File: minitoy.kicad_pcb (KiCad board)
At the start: 4 copper layers, 47.2 x 45 mm, 49 parts, among them J1 Conn_01x06, J2 PMOD1, J3 PMOD2, J4 USB_B_Micro, J5 PMOD3, U1 ICE40UP5K-SG48, U2 ESP-12E, U3 MIC5504-1.2YM5, U4 MIC5504-3.3YM5, U5 MIC5504-3.3YM5

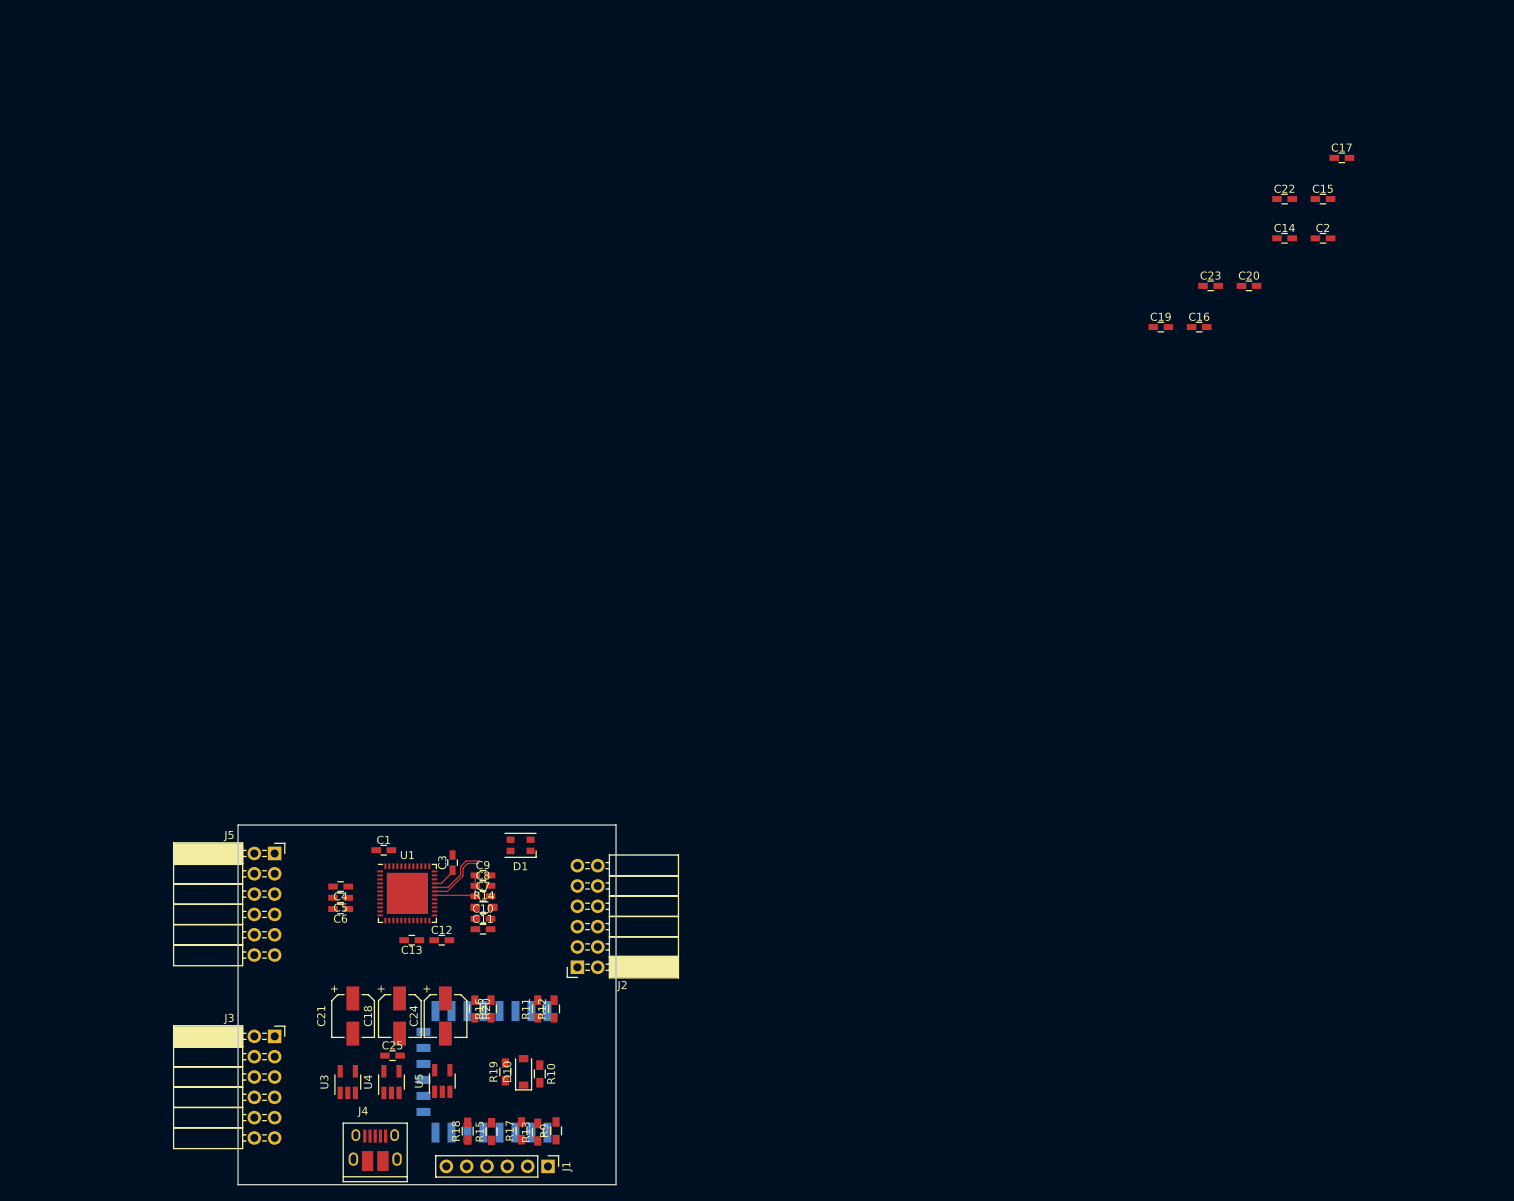
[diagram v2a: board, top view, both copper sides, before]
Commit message: More layout changes, remove a PMOD socket for easier routing
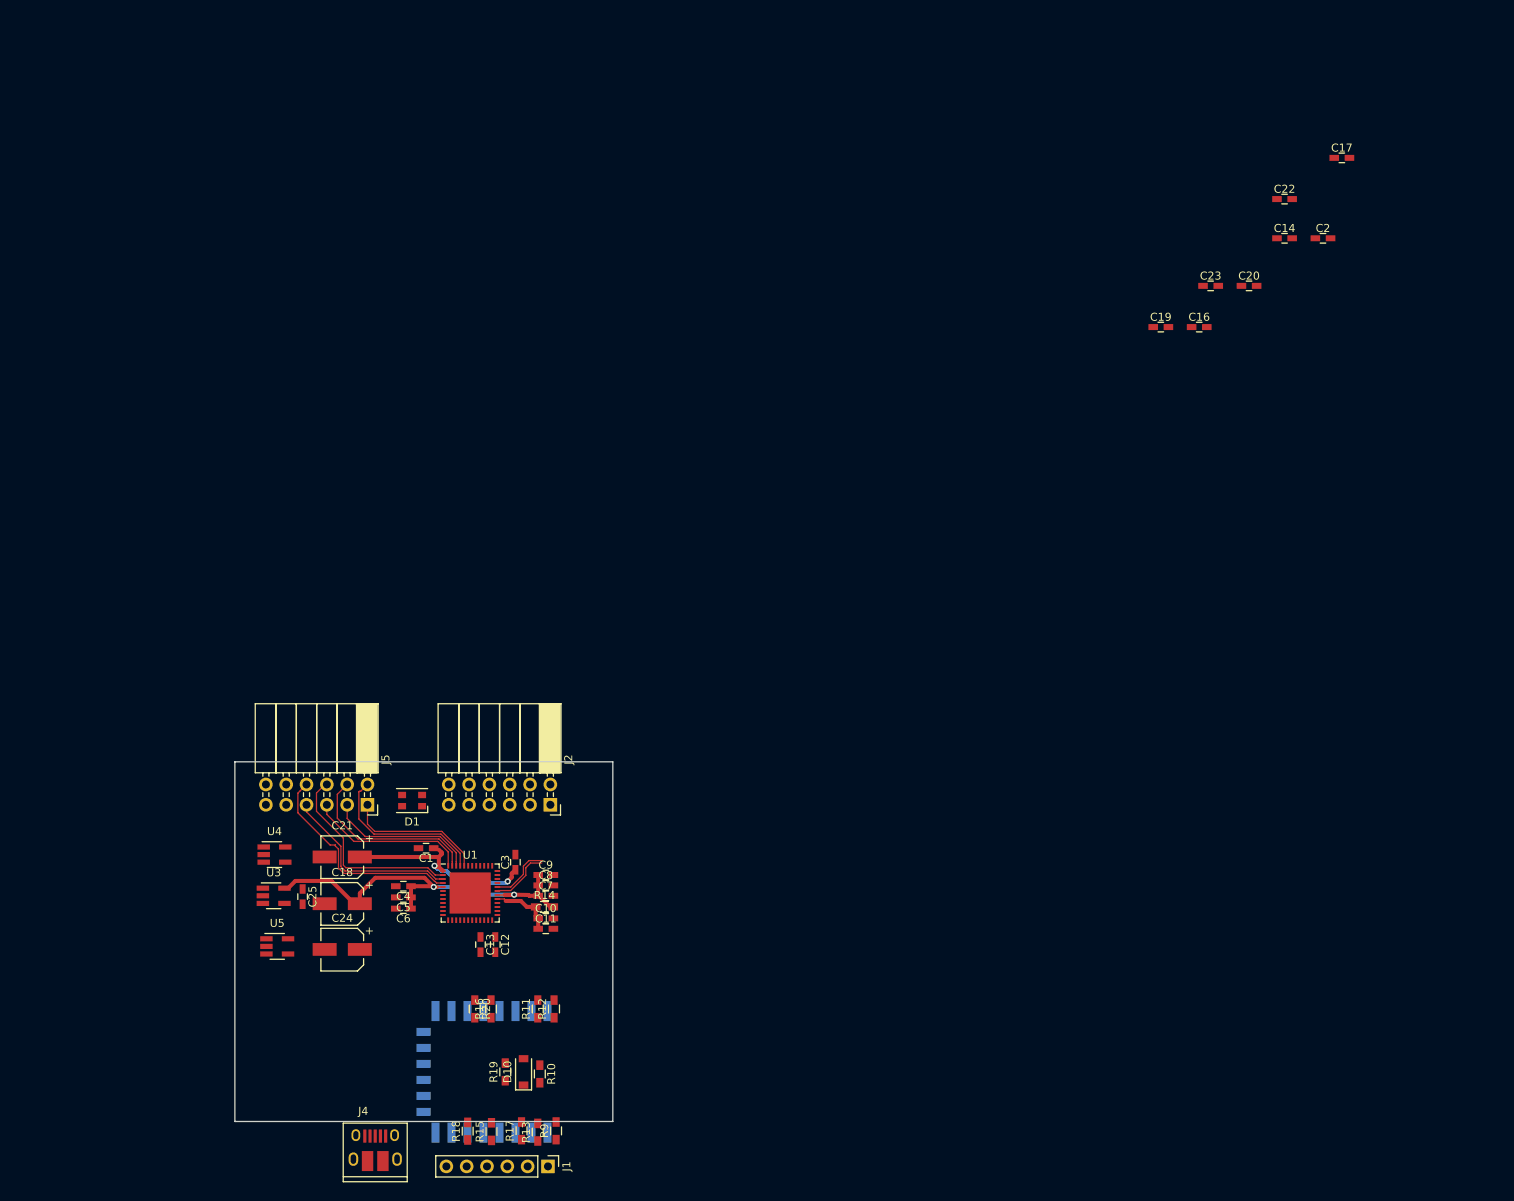
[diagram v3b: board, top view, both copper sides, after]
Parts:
- removed C15: 0.1uF, Capacitors_SMD:C_0603_HandSoldering
- removed J3: PMOD2, Socket_Strips:Socket_Strip_Angled_2x06_Pitch2.54mm
- J5: value PMOD3 -> PMOD2
- moved U4 32.0 mm to (96.5, 111.9), turned to 0 degrees
- moved U5 26.6 mm to (96.8, 123.4), turned to 0 degrees
- moved U3 25.1 mm to (96.4, 117.0), turned to 0 degrees
- moved C25 22.8 mm to (100.0, 117.2), turned to 270 degrees
- moved J2 20.6 mm to (131.0, 105.7), turned to 270 degrees
- moved C21 19.9 mm to (105.0, 112.2), turned to 180 degrees
- moved C18 15.8 mm to (105.0, 118.0), turned to 180 degrees
- moved C24 15.3 mm to (105.0, 123.8), turned to 180 degrees
- moved D1 14.7 mm to (113.7, 105.2)
- moved J5 13.1 mm to (108.1, 105.7), turned to 270 degrees
- moved C13 8.61 mm to (122.2, 123.2), turned to 270 degrees
- moved C10 7.85 mm to (130.4, 119.9)
- moved C11 7.85 mm to (130.4, 121.2)
- moved C7 7.85 mm to (130.4, 117.1)
- moved C8 7.85 mm to (130.4, 115.8)
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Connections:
- net Net-(C10-Pad1) renamed /VCCPLL
- J5 pad 1: PMOD-3.1 -> PMOD-2.1
- J5 pad 2: PMOD-3.7 -> PMOD-2.7
- J5 pad 3: PMOD-3.2 -> PMOD-2.2
- J5 pad 4: PMOD-3.8 -> PMOD-2.8
- J5 pad 5: PMOD-3.3 -> PMOD-2.3
- J5 pad 6: PMOD-3.9 -> PMOD-2.9
- J5 pad 7: PMOD-3.4 -> PMOD-2.4
- J5 pad 8: PMOD-3.10 -> PMOD-2.10
- U1 pad 10: PMOD-2.3 -> Net-(U1-Pad10)
- U1 pad 11: PMOD-2.4 -> Net-(U1-Pad11)
- U1 pad 12: PMOD-2.7 -> Net-(U1-Pad12)
- U1 pad 13: PMOD-2.8 -> Net-(U1-Pad13)
- U1 pad 18: PMOD-2.9 -> Net-(U1-Pad18)
- U1 pad 19: PMOD-2.10 -> Net-(U1-Pad19)
- U1 pad 2: PMOD-3.8 -> PMOD-2.9
- U1 pad 3: PMOD-3.9 -> PMOD-2.4
- U1 pad 4: PMOD-3.10 -> PMOD-2.10
- U1 pad 44: PMOD-3.1 -> PMOD-2.1
- U1 pad 45: PMOD-3.2 -> PMOD-2.7
- U1 pad 46: PMOD-3.3 -> PMOD-2.2
- U1 pad 47: PMOD-3.4 -> PMOD-2.8
- U1 pad 48: PMOD-3.7 -> PMOD-2.3
- U1 pad 6: PMOD-2.1 -> Net-(U1-Pad6)
- U1 pad 9: PMOD-2.2 -> Net-(U1-Pad9)
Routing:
- net +1V2: track 7.74 -> 50.3 mm, vias 0 -> 2
- net PMOD-2.10: track 0.00 -> 27.2 mm
- net PMOD-2.9: track 0.00 -> 25.1 mm
- net PMOD-2.4: track 0.00 -> 22.9 mm
- net PMOD-2.8: track 0.00 -> 22.6 mm
- net +3V3: track 3.07 -> 25.6 mm, vias 0 -> 2
- net PMOD-2.7: track 0.00 -> 20.9 mm
- net PMOD-2.3: track 0.00 -> 20.0 mm
- net PMOD-2.2: track 0.00 -> 18.7 mm
- net PMOD-2.1: track 0.00 -> 17.5 mm
- net /VCCPLL: track 0.00 -> 8.02 mm
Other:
- net class PWR: clearance 0.254 -> 0.1524

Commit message: Routing done, but cleanup needed
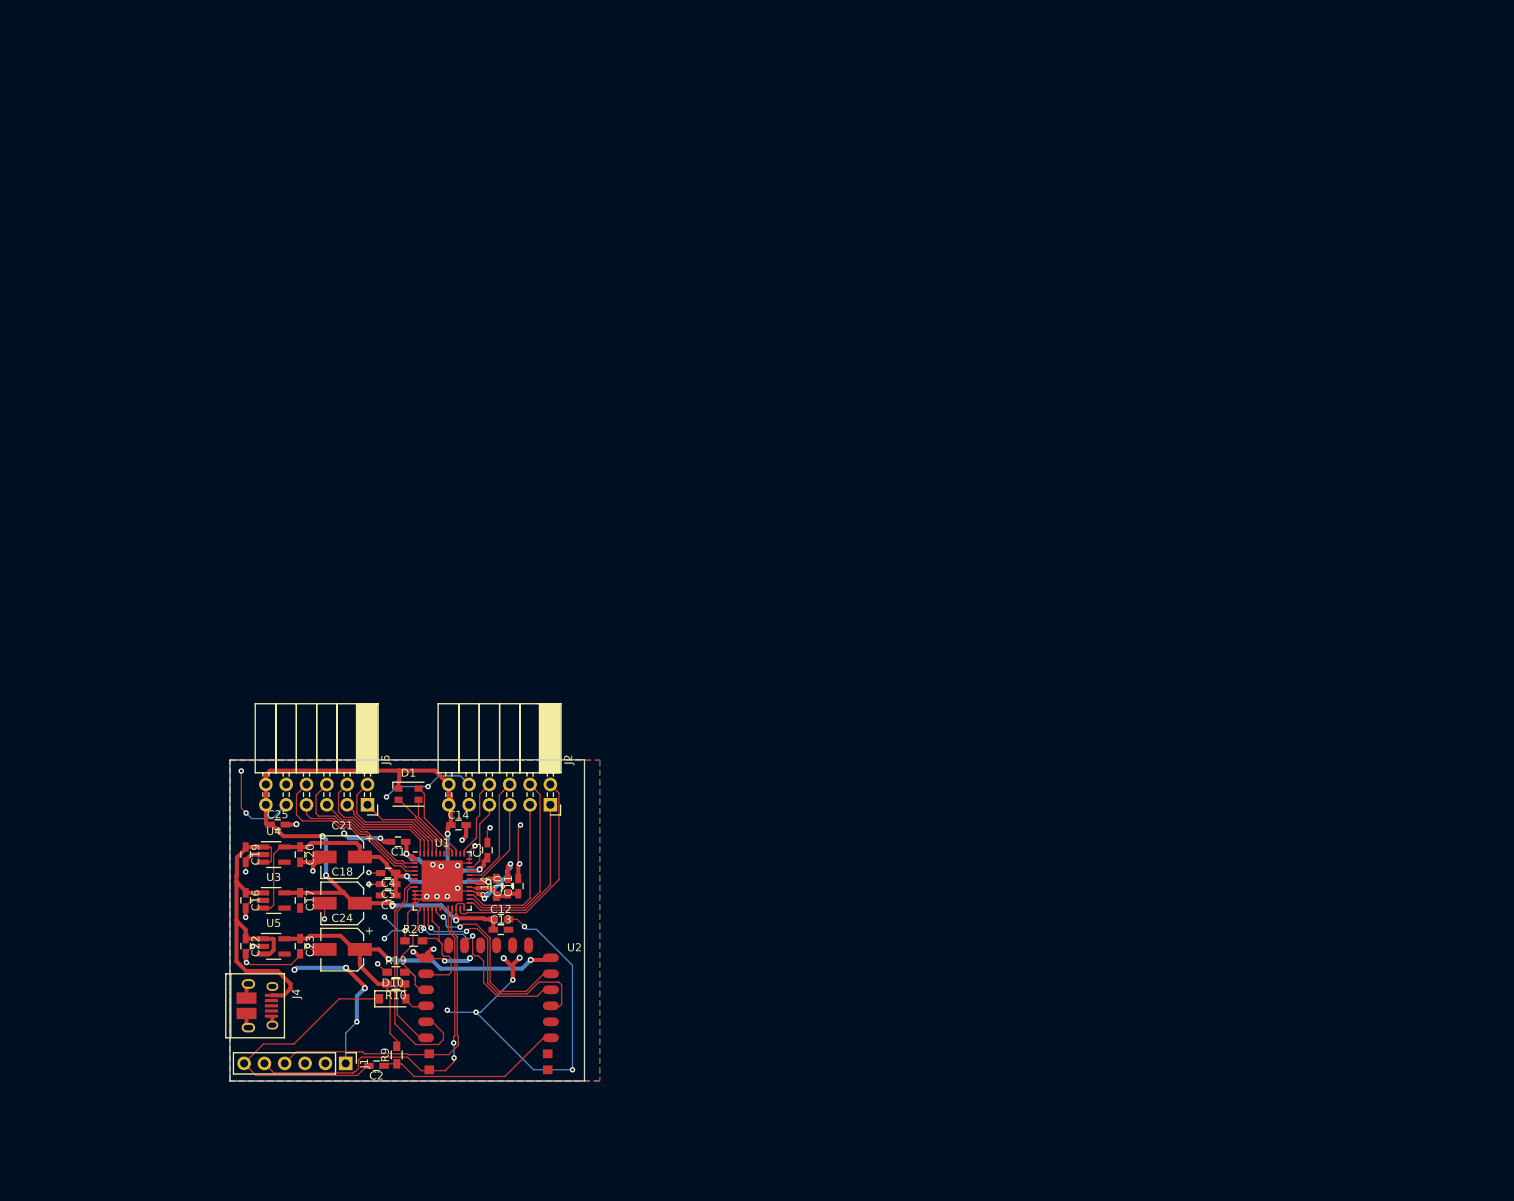
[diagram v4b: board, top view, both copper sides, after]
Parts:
- removed C7: 0.01uF, Capacitors_SMD:C_0603_HandSoldering
- removed C8: 0.1uF, Capacitors_SMD:C_0603_HandSoldering
- removed C9: 1uF, Capacitors_SMD:C_0603_HandSoldering
- removed R11, R12, R13, R15, R16, R17, R18: 100, Resistors_SMD:R_0603_HandSoldering
- C1, C13, C3: value 0.01uF -> 0.1uF
- U2: footprint RF_Modules:ESP-12E -> wifi_pants:ESP-12E-narrow; moved to F.Cu
- U3: value MIC5504-1.2YM5 -> MIC5504-3.3YM5
- U4: value MIC5504-3.3YM5 -> MIC5504-1.2YM5
- moved C22 160.0 mm to (92.9, 123.3), turned to 270 degrees
- moved C17 159.9 mm to (99.7, 117.6), turned to 270 degrees
- moved C2 157.2 mm to (109.2, 138.3), turned to 180 degrees
- moved C23 140.6 mm to (99.7, 123.3), turned to 270 degrees
- moved C16 139.1 mm to (92.9, 117.6), turned to 270 degrees
- moved C20 138.3 mm to (99.7, 111.9), turned to 270 degrees
- moved C19 132.0 mm to (92.9, 111.9), turned to 270 degrees
- moved C14 126.7 mm to (119.5, 108.2)
- moved J1 28.4 mm to (105.4, 138.0)
- moved J4 22.9 mm to (94.6, 130.8), turned to 270 degrees
- moved R9 22.1 mm to (111.8, 136.9)
- moved R10 21.2 mm to (111.7, 128.1), turned to 180 degrees
- moved D10 18.7 mm to (111.3, 129.9), turned to 0 degrees
- moved R19 18.5 mm to (111.7, 126.6), turned to 0 degrees
- moved R20 11.4 mm to (113.9, 122.7), turned to 0 degrees
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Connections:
- C17 pad 1: +1V2 -> +3V3
- C18 pad 1: +1V2 -> +3V3
- C20 pad 1: +3V3 -> +1V2
- C21 pad 1: +3V3 -> +1V2
- R19 pad 2: FPGA_PWR_EN -> FPGA_INT
- R20 pad 2: Net-(R16-Pad1) -> FPGA_CFG_SS
- U1 pad 10: Net-(U1-Pad10) -> GND
- U1 pad 11: Net-(U1-Pad11) -> GND
- U1 pad 12: Net-(U1-Pad12) -> GND
- U1 pad 13: Net-(U1-Pad13) -> FPGA_INT
- U1 pad 28: FPGA_INT -> GND
- U1 pad 35: Net-(U1-Pad35) -> GND
- U1 pad 36: Net-(U1-Pad36) -> GND
- U1 pad 9: Net-(U1-Pad9) -> GND
- U2 pad 16: Net-(R16-Pad1) -> FPGA_CFG_SS
- U2 pad 17: FPGA_PWR_EN -> FPGA_INT
- U2 pad 19: Net-(R11-Pad1) -> FPGA_CDONE
- U2 pad 20: Net-(R12-Pad1) -> FPGA_CRESET
- U2 pad 5: Net-(R17-Pad1) -> FPGA_CFG_SCLK
- U2 pad 6: Net-(R18-Pad1) -> FPGA_CFG_MISO
- U2 pad 7: Net-(R15-Pad1) -> FPGA_CFG_MOSI
- U3 pad 3: FPGA_PWR_EN -> +1V2
- U3 pad 5: +1V2 -> +3V3
- U4 pad 3: +1V2 -> VDD
- U4 pad 5: +3V3 -> +1V2
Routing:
- net GND: track 0.00 -> 204.1 mm, vias 0 -> 49
- net +3V3: track 25.6 -> 110.2 mm, vias 2 -> 7
- net +3.3VA: track 0.00 -> 50.0 mm, vias 0 -> 2
- net ESP_UART_TX: track 0.00 -> 46.6 mm, vias 0 -> 2
- net VDD: track 0.00 -> 45.2 mm
- net ESP_UART_RX: track 0.00 -> 41.3 mm
- net ESP_PROG: track 0.00 -> 37.0 mm
- net FPGA_CFG_SCLK: track 0.00 -> 30.8 mm, vias 0 -> 2
- net FPGA_CDONE: track 0.00 -> 29.7 mm
- net PMOD-1.7: track 0.00 -> 27.0 mm
- net FPGA_CFG_MISO: track 0.00 -> 25.2 mm, vias 0 -> 2
- net PMOD-1.8: track 0.00 -> 24.0 mm
- net FPGA_CFG_MOSI: track 0.00 -> 23.5 mm, vias 0 -> 2
- net Net-(C2-Pad1): track 0.00 -> 23.3 mm
- net FPGA_CRESET: track 0.00 -> 22.2 mm
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- added copper zone on B.Cu, net GND
- added copper zone on F.Cu, net GND
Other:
- board size 47.2 x 45 mm -> 44.3 x 40.2 mm
- copper layers 4 -> 2

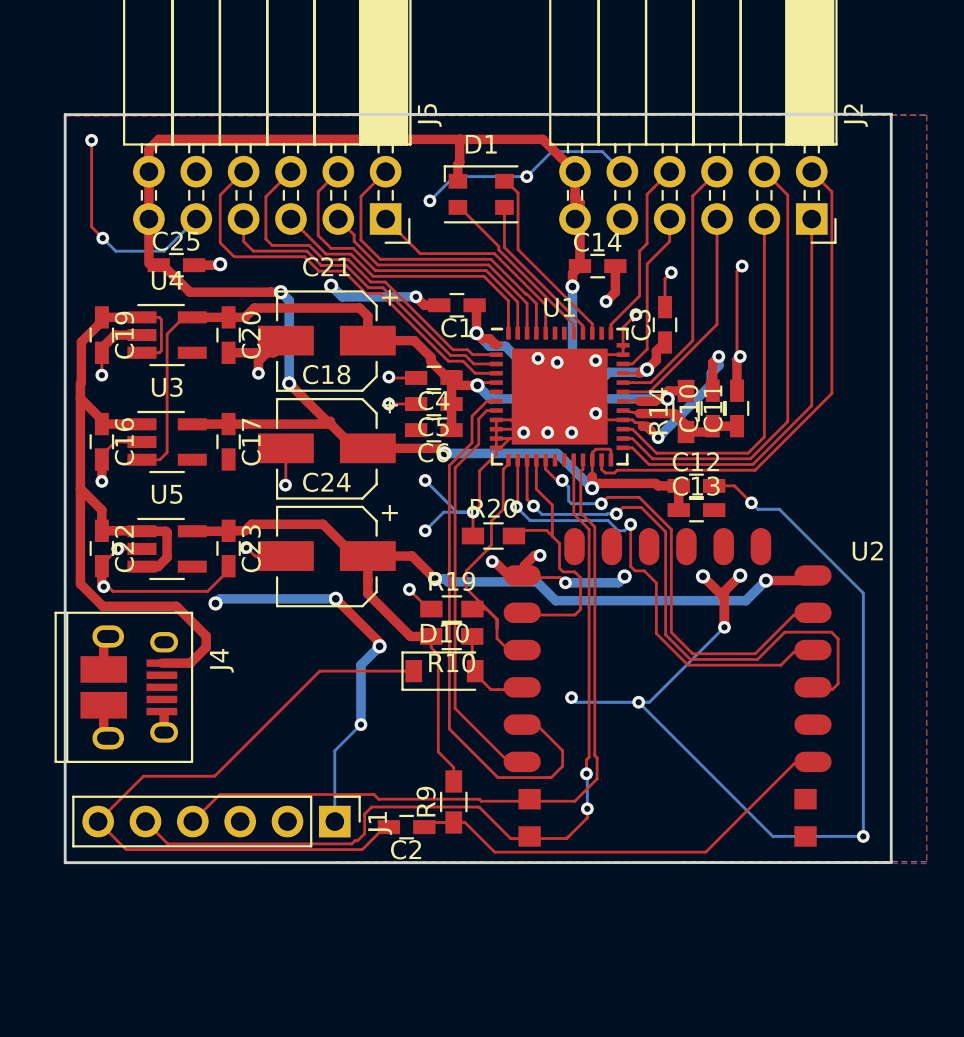
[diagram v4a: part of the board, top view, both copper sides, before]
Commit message: Routing complete.  Next up, fix silk.
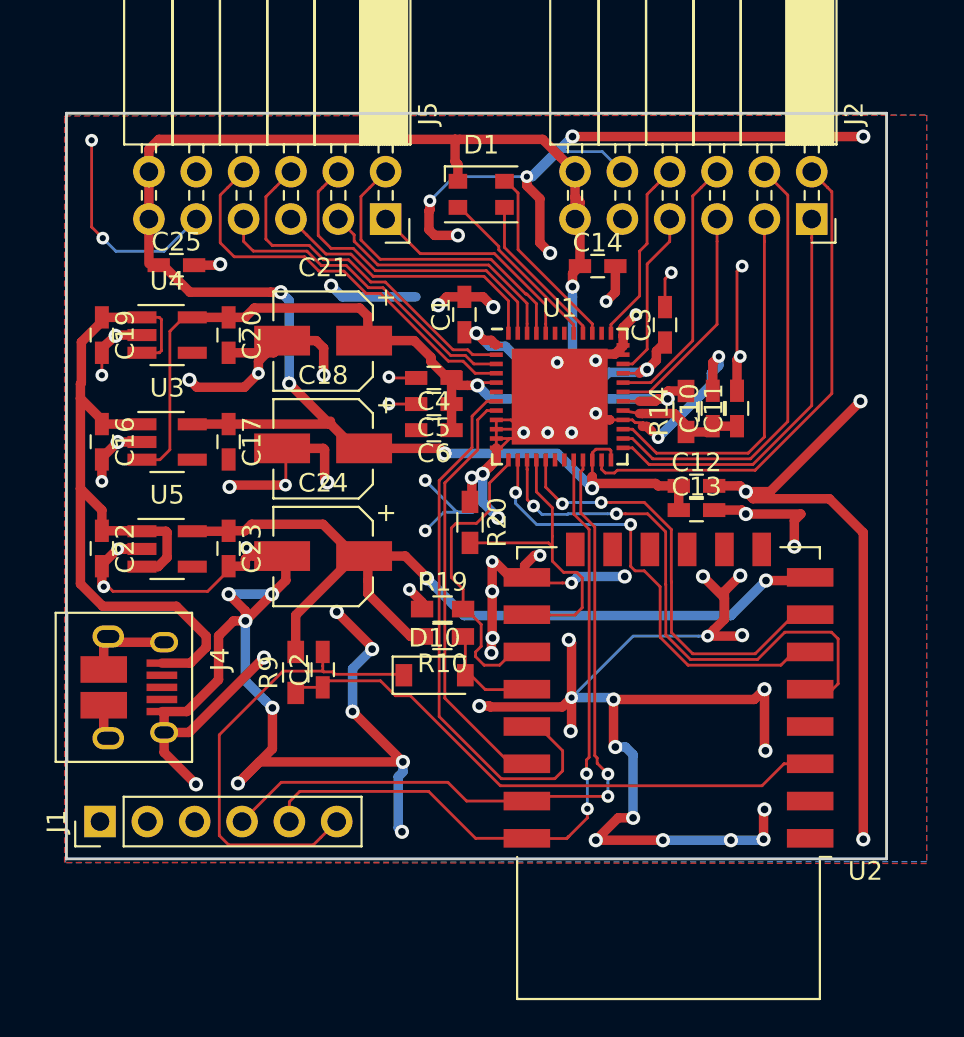
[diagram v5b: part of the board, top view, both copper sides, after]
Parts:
- U2: footprint wifi_pants:ESP-12E-narrow -> RF_Modules:ESP-12E
- moved J1 12.6 mm to (92.8, 138.0), turned to 90 degrees
- moved R9 11.0 mm to (103.3, 130.0)
- moved C2 9.57 mm to (104.8, 129.8), turned to 90 degrees
- moved U2 8.65 mm to (123.3, 135.4)
- moved R20 1.46 mm to (112.7, 122.0), turned to 270 degrees
- moved C1 0.64 mm to (112.3, 110.8), turned to 90 degrees
- moved D10 0.57 mm to (110.8, 130.2)
- moved R10 0.50 mm to (111.2, 128.1)
- moved R19 0.50 mm to (111.2, 126.6)
- moved C18 0.20 mm to (104.8, 118.0)
- moved C21 0.20 mm to (104.8, 112.2)
- moved C24 0.20 mm to (104.8, 123.8)
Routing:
- net GND: track 204.1 -> 354.0 mm, vias 49 -> 88
- net ESP_PROG: track 37.0 -> 24.9 mm
- net Net-(C2-Pad1): track 23.3 -> 30.7 mm
- net ESP_UART_TX: track 46.6 -> 39.4 mm
- net FPGA_INT: track 15.0 -> 17.3 mm
- net FPGA_CFG_SS: track 14.8 -> 17.1 mm
- net +3.3VA: track 50.0 -> 48.4 mm
- net ESP_UART_RX: track 41.3 -> 39.7 mm, vias 0 -> 2
- net +3V3: track 110.2 -> 109.3 mm
- net FPGA_CDONE: track 29.7 -> 30.3 mm
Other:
- board size 44.3 x 40.2 mm -> 44 x 40 mm
